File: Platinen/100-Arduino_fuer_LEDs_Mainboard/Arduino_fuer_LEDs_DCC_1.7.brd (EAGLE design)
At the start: 98.5 x 72.1 mm, 115 parts, among them IC1 7805, IC2 LM393N, J1 Tag/Nacht, U1 WS2812_MODUL, U2 LED NANO, U3 DCC NANO, U4 WS2812_MODUL, X1 RJ10, X2 AK500/2+M, X3 MAB 5SH Conrad: 738247 - VQ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

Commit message: New Mainboard V.:1.7
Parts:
- added IC3: 74LVC1G125DBV, 74xx-little-de:SOT23-5
- added R2: 47, rcl:0204/7
- added R9: 10K, rcl:0204/5
- added SJ2: SOLDERJUMPERNO, SparkFun-Retired:SJ_2S-NO
- moved R28 1.27 mm to (40.6, 22.9)
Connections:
- removed net N$53: O4.4
- new net N$22: O3.4, O4.2
- new net N$31: IC3.2, R26.2, SJ2.1, U3.TX0
- new net N$33: IC3.4, R2.1
- new net N$34: R2.2, SJ2.2, U2.RX1
- net +5V: now also IC3.5, R9.2
- net GND: now also IC3.3
- net N$3: now also IC3.1, R9.1, U3.A5; no longer R26.2, U2.RX1, U3.TX0
- net N$52: now also O4.4; no longer O3.4, O4.2
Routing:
- net N$31: track 0.00 -> 32.6 mm
- net N$34: track 0.00 -> 27.8 mm
- net N$33: track 0.00 -> 16.0 mm
- net N$52: track 81.0 -> 67.9 mm
- net GND: track 667.8 -> 678.8 mm, vias 4 -> 5
- net N$22: track 0.00 -> 10.6 mm
- net N$3: track 29.1 -> 24.3 mm, vias 0 -> 1
- net N$18: track 17.3 -> 21.9 mm
- net N$27: track 56.7 -> 59.2 mm
- net D6: track 66.9 -> 68.3 mm
- net SX_T0: track 43.9 -> 42.6 mm
- net +5V: track 501.0 -> 501.8 mm
- net N$42: track 6.05 -> 6.58 mm

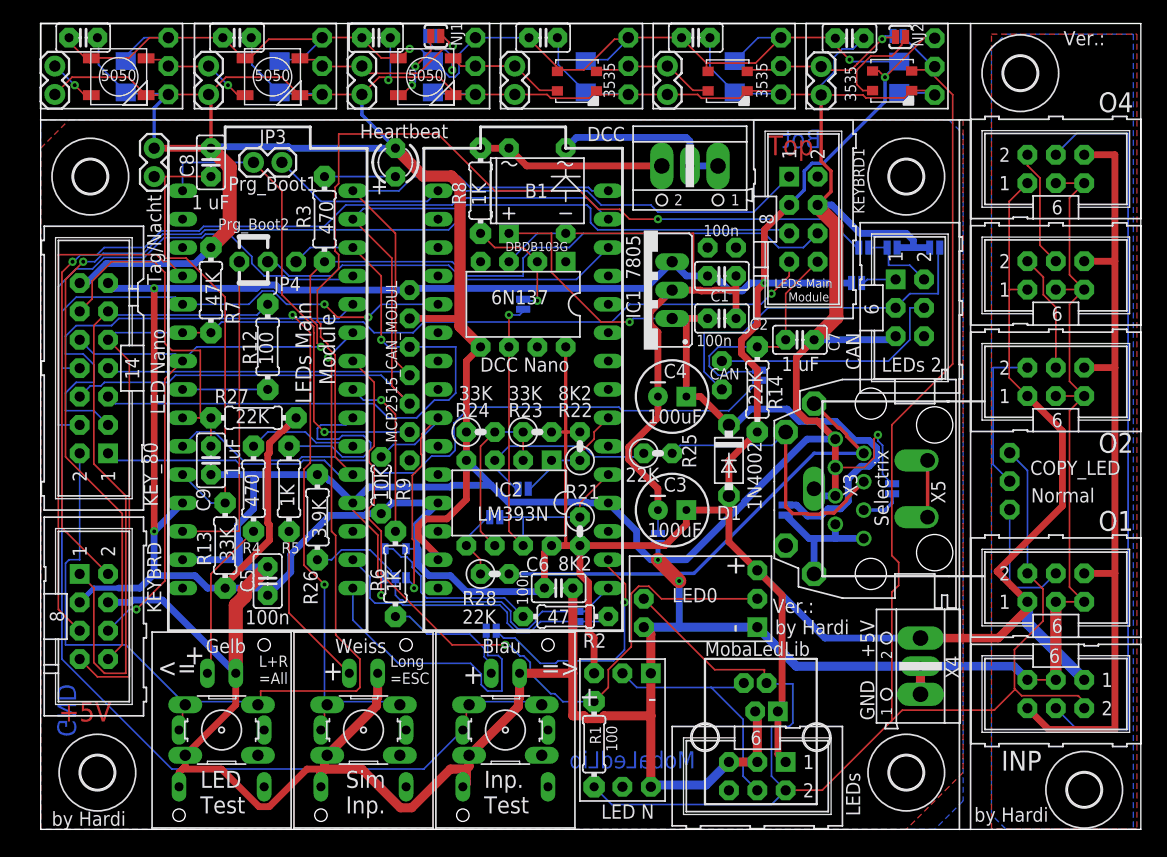
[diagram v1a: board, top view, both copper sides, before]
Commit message: Moved IC3
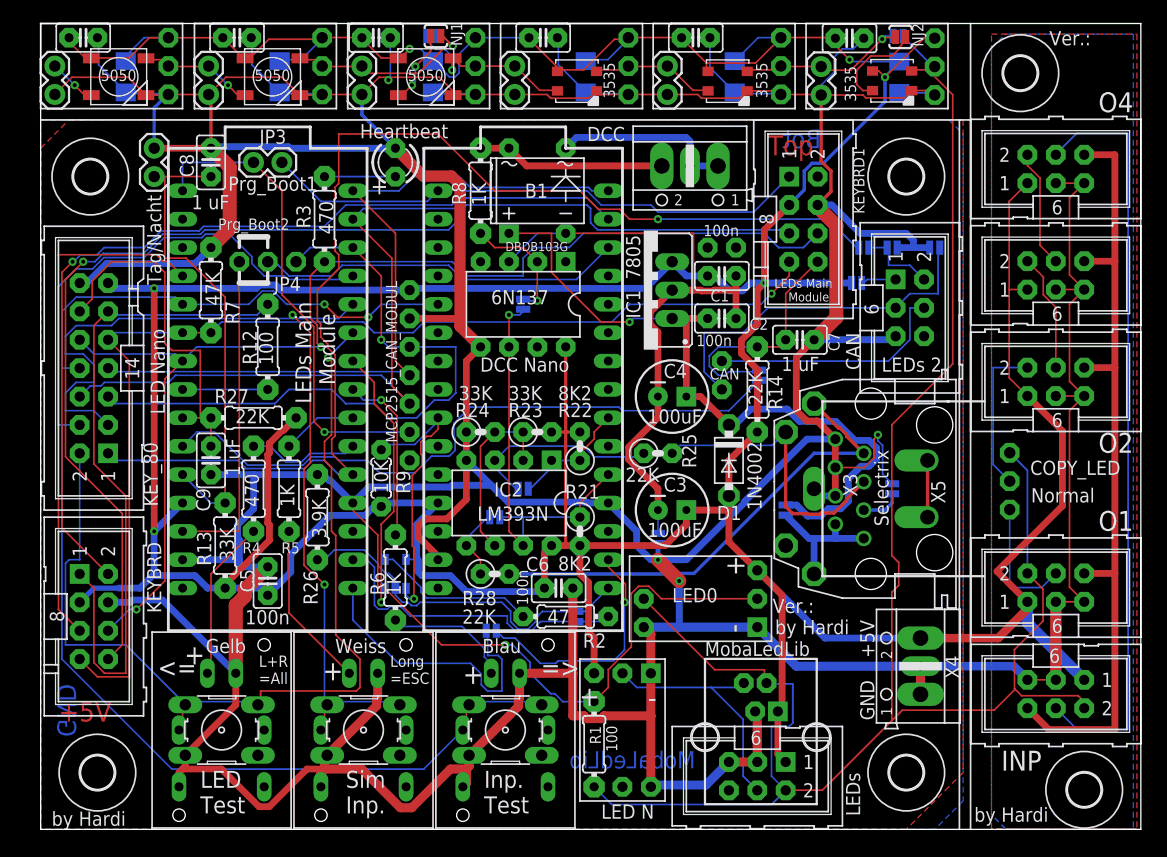
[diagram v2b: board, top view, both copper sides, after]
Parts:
- moved IC3 0.95 mm to (31.8, 22.9)
- moved R9 0.64 mm to (30.5, 31.4)
- moved R6 0.32 mm to (31.8, 22.5)
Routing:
- net D4: track 18.3 -> 6.77 mm
- net N$33: track 16.0 -> 14.8 mm
- net N$3: track 24.3 -> 25.4 mm
- net D10: track 58.8 -> 59.8 mm
- net N$34: track 27.8 -> 28.7 mm
- net D6: track 68.3 -> 69.0 mm
- net D2: track 106.6 -> 107.2 mm
- net D7: track 84.9 -> 85.4 mm
